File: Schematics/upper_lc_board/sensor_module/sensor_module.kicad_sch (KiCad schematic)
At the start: 42 parts, among them J3 PT2, J4 PT1, J5 HALL, J7 TC, U6 LM324DT, U7 ADC_ADS131M04IPWR

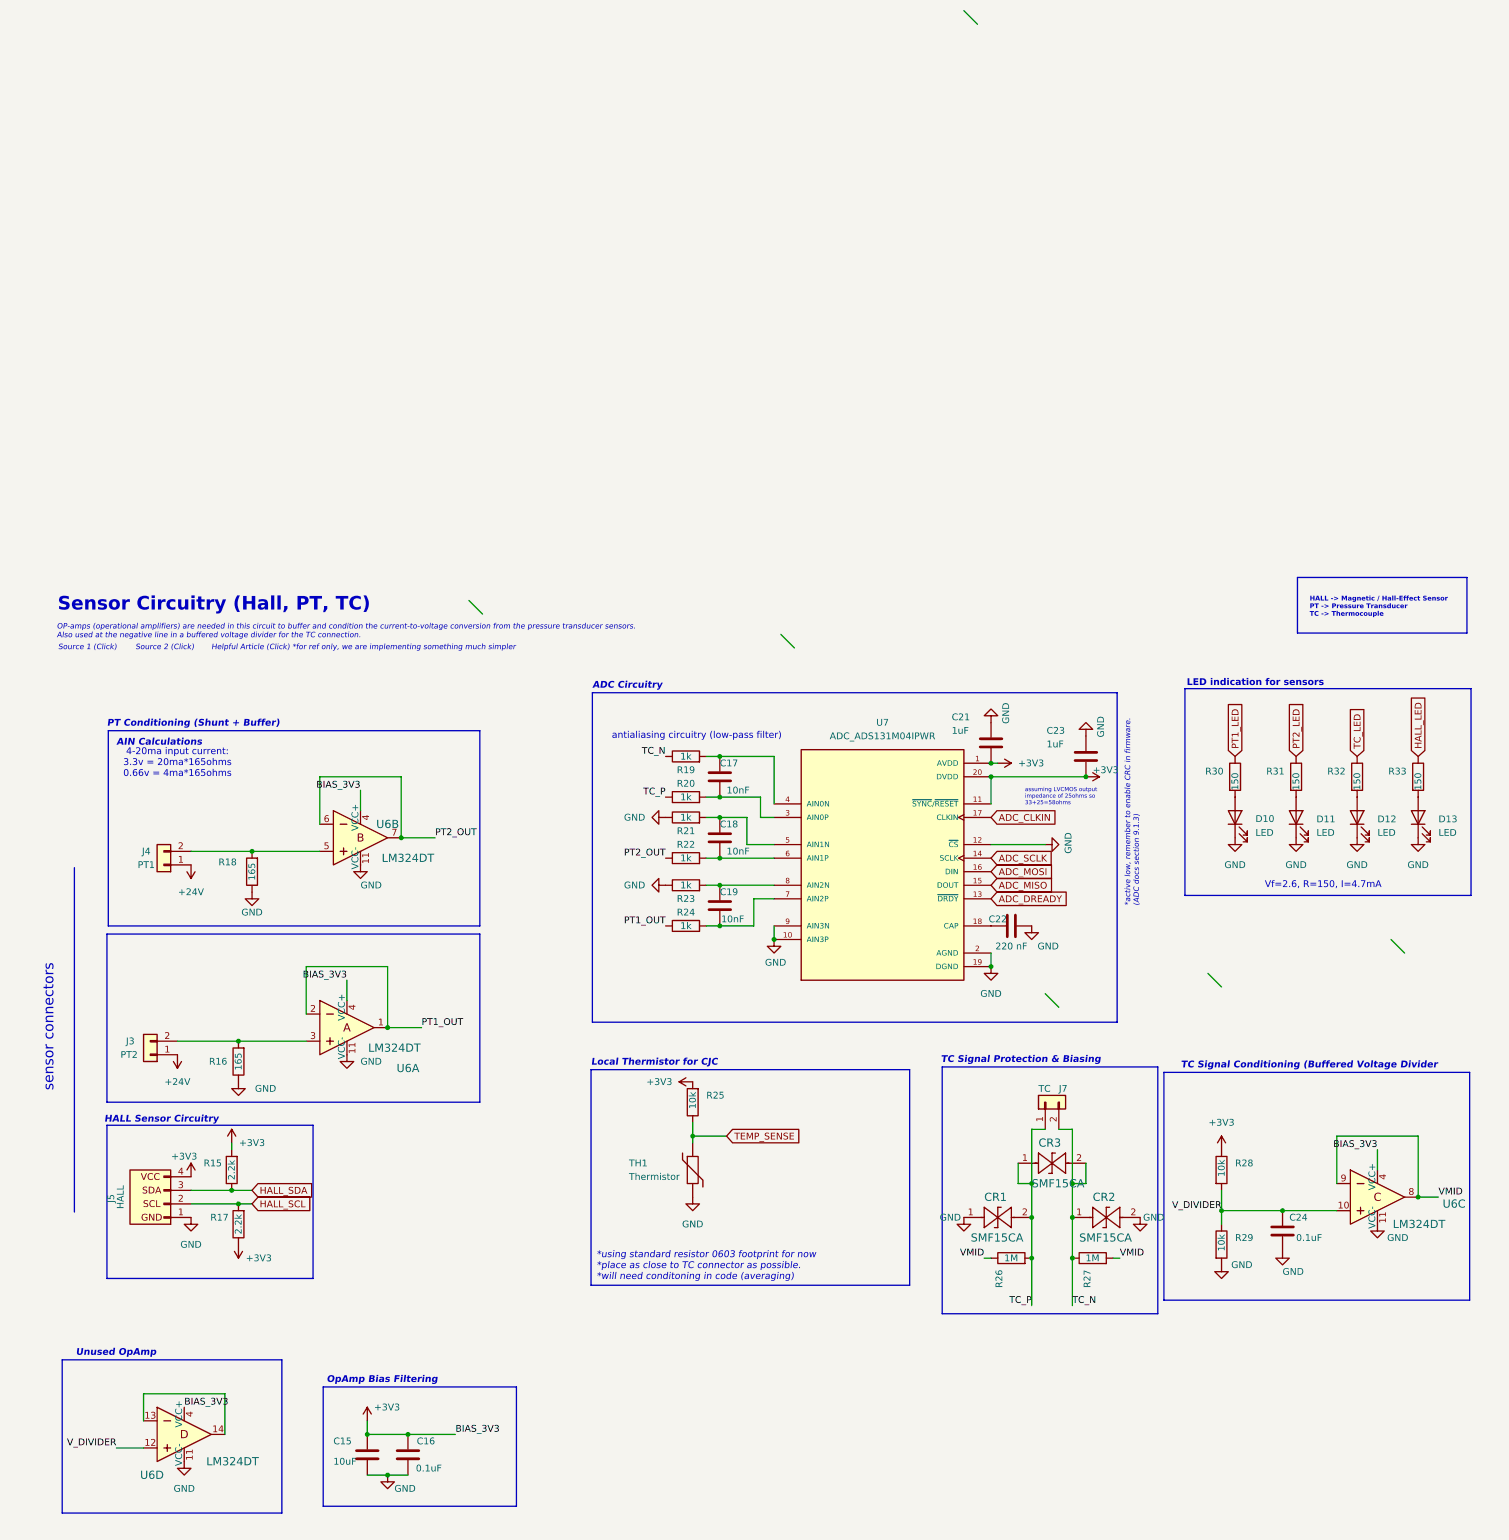
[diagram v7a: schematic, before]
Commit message: updated opamp, 24v tvs diode, and excluded usbc antenna overlap error
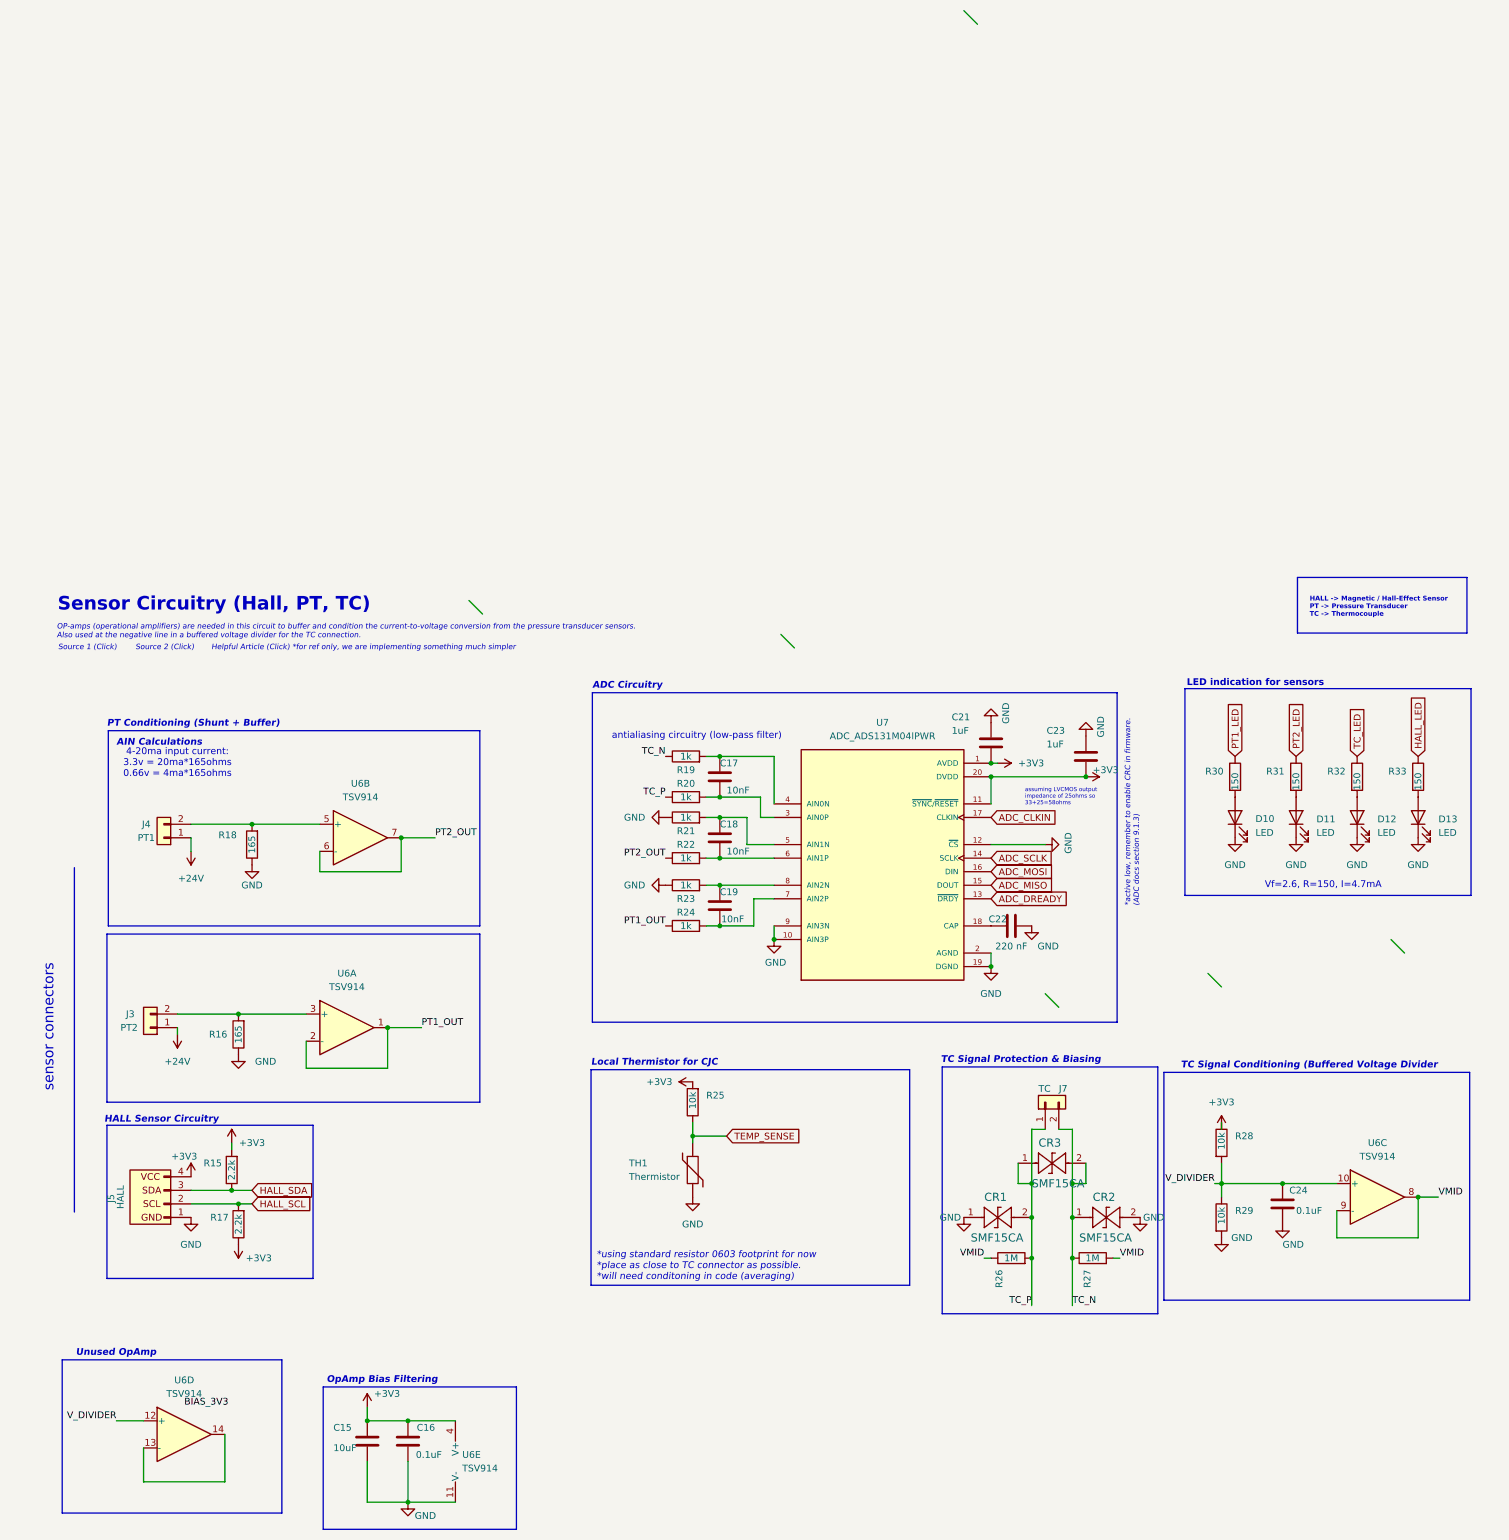
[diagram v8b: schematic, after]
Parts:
- removed U6: LM324DT, digikey-footprints:SOIC-14_W3.9mm, symbol dk_Linear-Amplifiers-Instrumentation-OP-Amps-Buffer-Amps:LM324DT
- added U6: TSV914, digikey-footprints:SOIC-14_W3.9mm, symbol Amplifier_Operational:TSV914
- C17, C18, C19: LCSC C1589 -> C76599
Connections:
- net +3V3: now also U6.4 (V+)
- net GND: now also U6.11 (V-)
- net PT1_OUT: now also U6.1, U6.2 (-)
- net PT2_OUT: now also U6.6 (-), U6.7
- net VMID: now also U6.8, U6.9 (-)
- net V_DIVIDER: now also U6.10 (+), U6.12 (+)
- net at J3.2 (Pin_2), R16.2: now also U6.3 (+)
- net at J4.2 (Pin_2), R18.2: now also U6.5 (+)
- new net: U6.13 (-), U6.14
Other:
- moved on the sheet: C15, C16, C24, J3, J4, R16, R18, R28, R29
